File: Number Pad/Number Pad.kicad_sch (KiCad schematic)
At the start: 44 parts, among them J1 Conn_01x05_Female, J2 Conn_01x05_Male

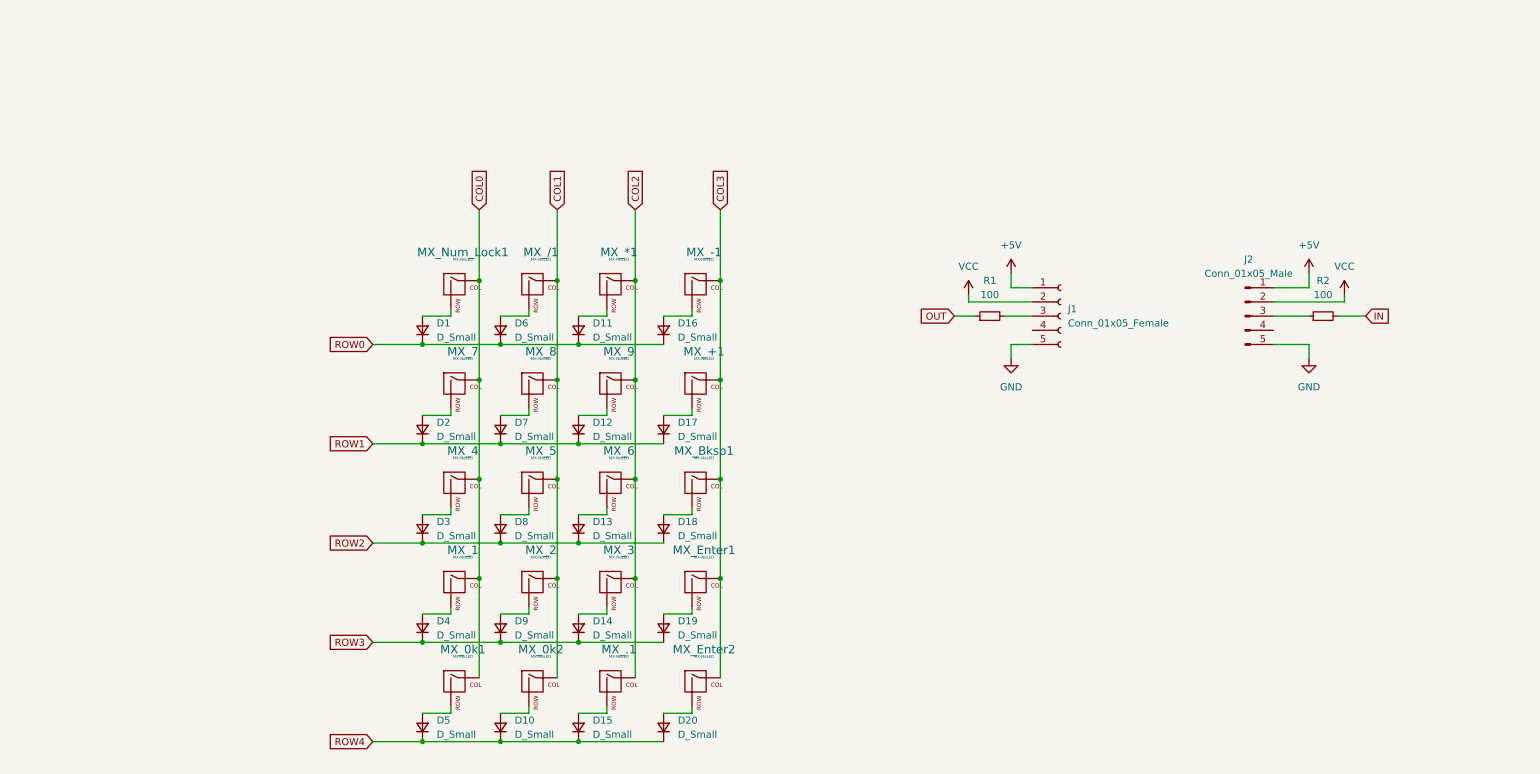
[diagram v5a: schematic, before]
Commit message: Updated connectors and footprints
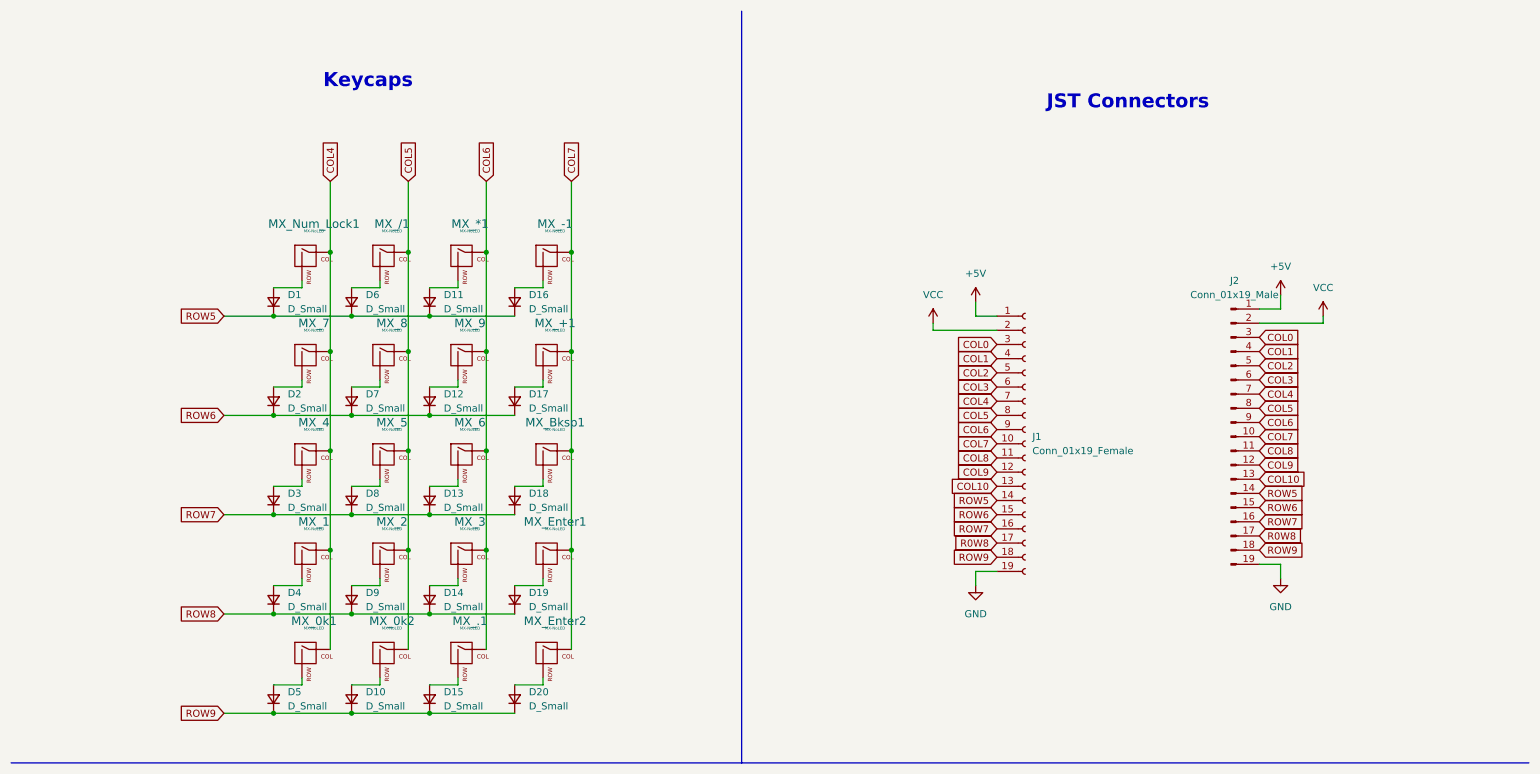
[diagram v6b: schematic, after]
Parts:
- removed J1: Conn_01x05_Female, Connector_JST:JST_PH_S5B-PH-K_1x05_P2.00mm_Horizontal, symbol Connector:Conn_01x05_Female
- removed J2: Conn_01x05_Male, Connector_JST:JST_PH_S5B-PH-K_1x05_P2.00mm_Horizontal, symbol Connector:Conn_01x05_Male
- removed R1, R2: 100, Resistor_SMD:R_0805_2012Metric, symbol Device:R_Small
- added J1: Conn_01x19_Female, Connector_JST:JST_SH_SM20B-SRSS-TB_1x20-1MP_P1.00mm_Horizontal, symbol Connector:Conn_01x19_Female
- added J2: Conn_01x19_Male, Connector_JST:JST_SH_SM20B-SRSS-TB_1x20-1MP_P1.00mm_Horizontal, symbol Connector:Conn_01x19_Male
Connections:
- net +5V: now also J1.1 (Pin_1), J2.1 (Pin_1)
- net COL0: now also J1.3 (Pin_3), J2.3 (Pin_3); no longer MX_0k1.1 (COL), MX_1.1 (COL), MX_4.1 (COL), MX_7.1 (COL), MX_Num_Lock1.1 (COL)
- net COL1: now also J1.4 (Pin_4), J2.4 (Pin_4); no longer MX_/1.1 (COL), MX_0k2.1 (COL), MX_2.1 (COL), MX_5.1 (COL), MX_8.1 (COL)
- net COL2: now also J1.5 (Pin_5), J2.5 (Pin_5); no longer MX_*1.1 (COL), MX_.1.1 (COL), MX_3.1 (COL), MX_6.1 (COL), MX_9.1 (COL)
- net COL3: now also J1.6 (Pin_6), J2.6 (Pin_6); no longer MX_+1.1 (COL), MX_-1.1 (COL), MX_Bksp1.1 (COL), MX_Enter1.1 (COL), MX_Enter2.1 (COL)
- net GND: now also J1.19 (Pin_19), J2.19 (Pin_19)
- net VCC: now also J1.2 (Pin_2), J2.2 (Pin_2)
- net ROW0 renamed ROW5
- net ROW5: now also J1.14 (Pin_14), J2.14 (Pin_14)
- net ROW1 renamed ROW6
- net ROW6: now also J1.15 (Pin_15), J2.15 (Pin_15)
- net ROW2 renamed ROW7
- net ROW7: now also J1.16 (Pin_16), J2.16 (Pin_16)
- net ROW3 renamed ROW8
- net ROW4 renamed ROW9
- net ROW9: now also J1.18 (Pin_18), J2.18 (Pin_18)
- new net COL10: J1.13 (Pin_13), J2.13 (Pin_13)
- new net COL4: J1.7 (Pin_7), J2.7 (Pin_7), MX_0k1.1 (COL), MX_1.1 (COL), MX_4.1 (COL), MX_7.1 (COL), MX_Num_Lock1.1 (COL)
- new net COL5: J1.8 (Pin_8), J2.8 (Pin_8), MX_/1.1 (COL), MX_0k2.1 (COL), MX_2.1 (COL), MX_5.1 (COL), MX_8.1 (COL)
- new net COL6: J1.9 (Pin_9), J2.9 (Pin_9), MX_*1.1 (COL), MX_.1.1 (COL), MX_3.1 (COL), MX_6.1 (COL), MX_9.1 (COL)
- new net COL7: J1.10 (Pin_10), J2.10 (Pin_10), MX_+1.1 (COL), MX_-1.1 (COL), MX_Bksp1.1 (COL), MX_Enter1.1 (COL), MX_Enter2.1 (COL)
- new net COL8: J1.11 (Pin_11), J2.11 (Pin_11)
- new net COL9: J1.12 (Pin_12), J2.12 (Pin_12)
- new net R0W8: J1.17 (Pin_17), J2.17 (Pin_17)
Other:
- note added: "JST Connectors"
- note added: "Keycaps"
- moved on the sheet: D1, D10, D11, D12, D13, D14, D15, D16, D17, D18, D19, D2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

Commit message: Finished routing
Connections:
- net R0W8 is gone; now on net ROW8: J1.17 (Pin_17), J2.17 (Pin_17)
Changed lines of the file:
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@@
     )
   )
-  (global_label "R0W8" (shape input) (at 189.23 107.95 180) (fields_autoplaced)
+  (global_label "ROW8" (shape input) (at 189.23 107.95 180) (fields_autoplaced)
     (effects (font (size 1.27 1.27)) (justify right))
-    (property "Intersheet References" "${INTERSHEET_REFS}" (id 0) (at 181.6764 107.8706 0)
+    (property "Intersheet References" "${INTERSHEET_REFS}" (id 0) (at 181.5555 107.8706 0)
       (effects (font (size 1.27 1.27)) (justify right) hide)
     )
@@
     )
   )
-  (global_label "R0W8" (shape input) (at 236.22 106.68 0) (fields_autoplaced)
+  (global_label "ROW8" (shape input) (at 236.22 106.68 0) (fields_autoplaced)
     (effects (font (size 1.27 1.27)) (justify left))
-    (property "Intersheet References" "${INTERSHEET_REFS}" (id 0) (at 243.7736 106.6006 0)
+    (property "Intersheet References" "${INTERSHEET_REFS}" (id 0) (at 243.8945 106.6006 0)
       (effects (font (size 1.27 1.27)) (justify left) hide)
     )

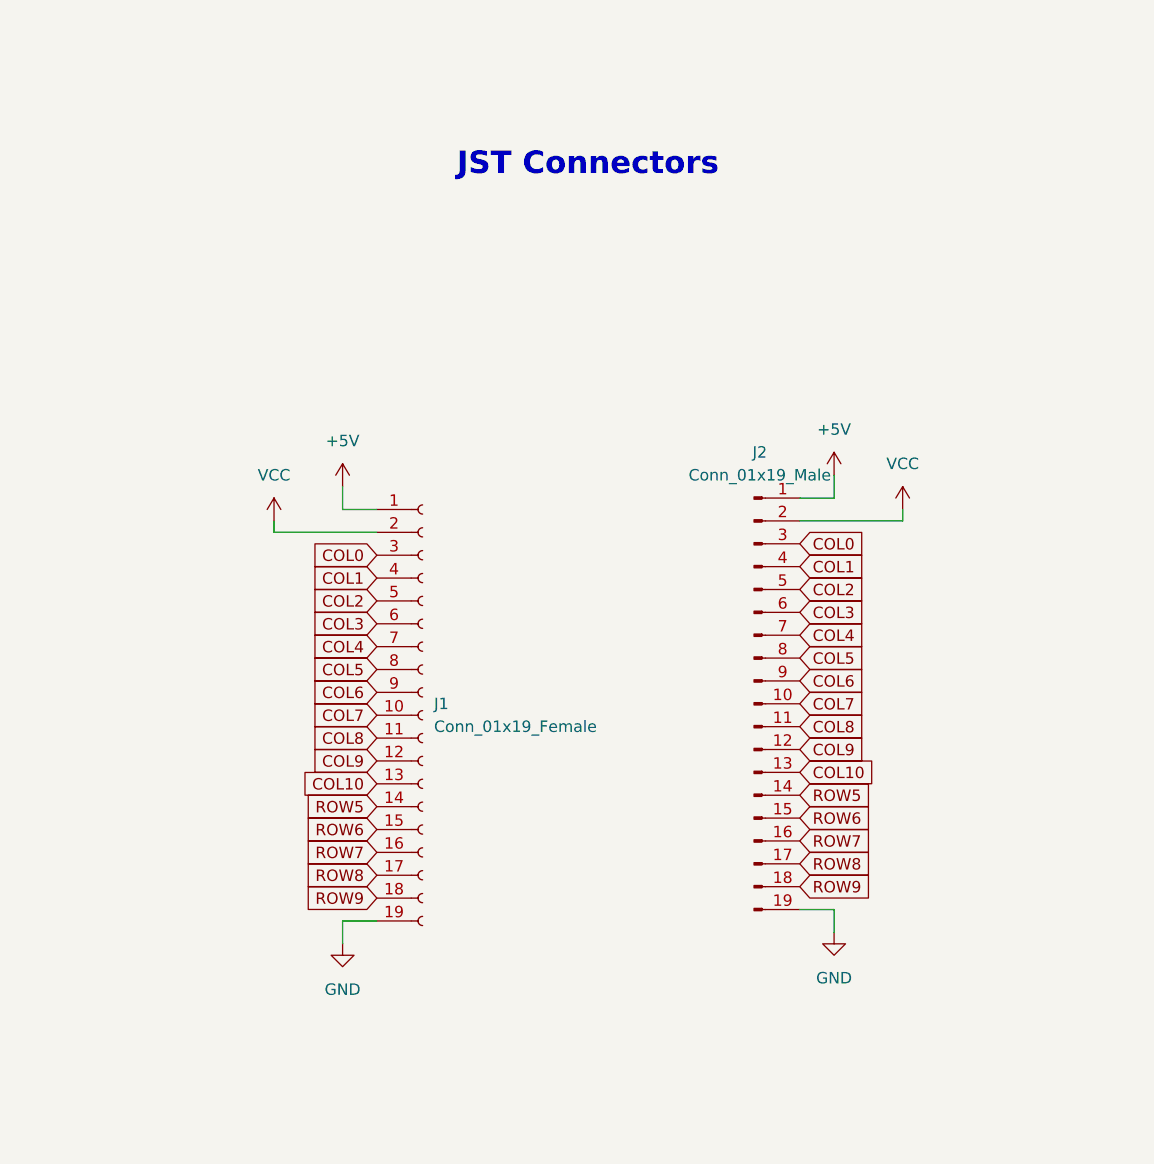
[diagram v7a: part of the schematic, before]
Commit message: Updated connectors on schematic
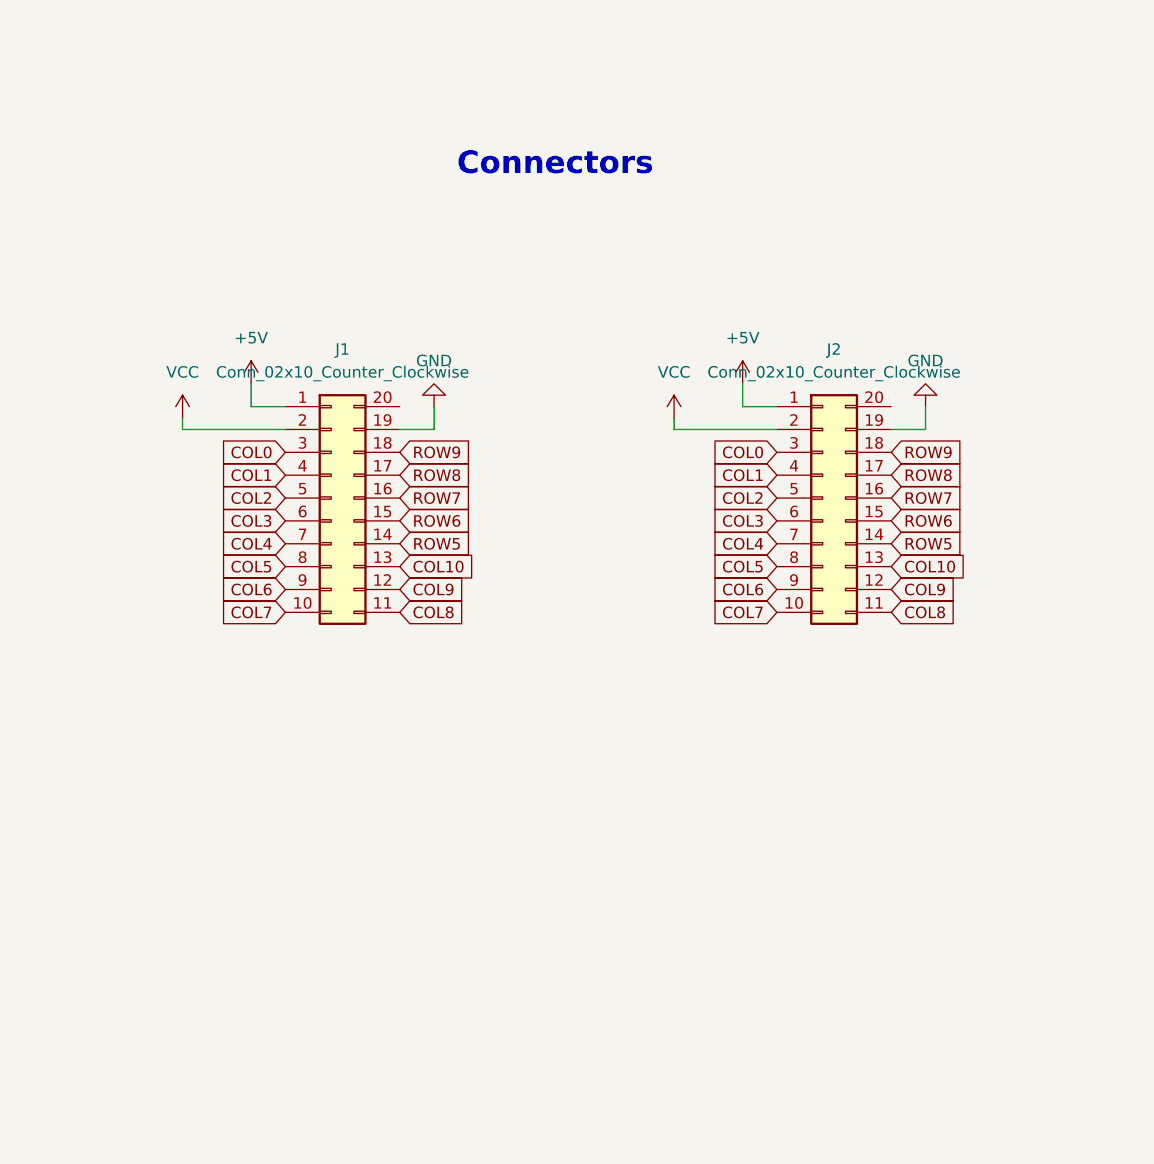
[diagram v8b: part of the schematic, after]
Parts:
- removed J1: Conn_01x19_Female, Connector_JST:JST_SH_SM20B-SRSS-TB_1x20-1MP_P1.00mm_Horizontal, symbol Connector:Conn_01x19_Female
- removed J2: Conn_01x19_Male, Connector_JST:JST_SH_SM20B-SRSS-TB_1x20-1MP_P1.00mm_Horizontal, symbol Connector:Conn_01x19_Male
- added J1: Conn_02x10_Counter_Clockwise, Connector_PinHeader_2.54mm:PinHeader_2x10_P2.54mm_Horizontal, symbol Connector_Generic:Conn_02x10_Counter_Clockwise
- added J2: Conn_02x10_Counter_Clockwise, Connector_PinSocket_2.54mm:PinSocket_2x10_P2.54mm_Horizontal, symbol Connector_Generic:Conn_02x10_Counter_Clockwise
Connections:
- net +5V: now also J1.1 (Pin_1), J2.1 (Pin_1)
- net COL0: now also J1.3 (Pin_3), J2.3 (Pin_3)
- net COL1: now also J1.4 (Pin_4), J2.4 (Pin_4)
- net COL10: now also J1.13 (Pin_13), J2.13 (Pin_13)
- net COL2: now also J1.5 (Pin_5), J2.5 (Pin_5)
- net COL3: now also J1.6 (Pin_6), J2.6 (Pin_6)
- net COL4: now also J1.7 (Pin_7), J2.7 (Pin_7)
- net COL5: now also J1.8 (Pin_8), J2.8 (Pin_8)
- net COL6: now also J1.9 (Pin_9), J2.9 (Pin_9)
- net COL7: now also J1.10 (Pin_10), J2.10 (Pin_10)
- net COL8: now also J1.11 (Pin_11), J2.11 (Pin_11)
- net COL9: now also J1.12 (Pin_12), J2.12 (Pin_12)
- net GND: now also J1.19 (Pin_19), J2.19 (Pin_19)
- net ROW5: now also J1.14 (Pin_14), J2.14 (Pin_14)
- net ROW6: now also J1.15 (Pin_15), J2.15 (Pin_15)
- net ROW7: now also J1.16 (Pin_16), J2.16 (Pin_16)
- net ROW8: now also J1.17 (Pin_17), J2.17 (Pin_17)
- net ROW9: now also J1.18 (Pin_18), J2.18 (Pin_18)
- net VCC: now also J1.2 (Pin_2), J2.2 (Pin_2)
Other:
- note added: "Connectors"
- note removed: "JST Connectors"
